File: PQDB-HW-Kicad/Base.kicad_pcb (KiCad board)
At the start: 2 copper layers, 146.1 x 141 mm, 71 parts, among them Q101 BC847, Q102 BC847, Q201 BC847, Q301 BC847, Q302 BC847, Q303 BC847, Q304 BC847, SW101 BTN-01, SW102 BTN-01, SW103 BTN-01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

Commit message: Add files via upload
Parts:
- added G***: LOGO, bibliotecas:OSHW_GRANDE, F.Cu at (181.5, 104.6)
- added P101: EXT_I2C, bibliotecas:EXT_I2C, F.Cu at (65.8, 139.1)
- added R105: 1k, bibliotecas:HW_Resistor, F.Cu at (107.7, 126.7)
- added R106: 1k, bibliotecas:HW_Resistor, F.Cu at (154.7, 126.7)
- G***: moved to F.Cu
- RV201, RV401: value POT -> POT_DUPLO; footprint HW_Potenciometro_2 -> bibliotecas:HW_Potenciometro_2_Duplo
- X701: footprint Crystals:Crystal_Round_Horizontal_2mm -> bibliotecas:Crystal_Round_Horizontal_2mm
- moved G*** 12.7 mm to (181.2, 82.4)
- moved R503 7.83 mm to (162.2, 45.3)
- moved R502 7.78 mm to (166.4, 45.3)
- moved R501 7.77 mm to (170.7, 45.3)
- moved RGB501 6.21 mm to (165.7, 34.9)
- moved Q101 6.08 mm to (72.5, 147.1)
- moved BZ201 5.17 mm to (194.2, 31.7)
- moved R201 5.14 mm to (183.2, 47.4)
- moved C701 4.45 mm to (83.1, 125.6)
- moved U401 4.41 mm to (75.8, 32.1)
- moved R407 4.22 mm to (168.5, 29.7)
- moved R301 3.02 mm to (126.9, 83.4)
- moved R312 2.95 mm to (126.8, 63.5)
- moved R305 2.94 mm to (126.9, 100.4)
- moved R306 2.94 mm to (126.9, 104.2)
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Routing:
- net +5V: track 416.2 -> 461.6 mm
- net /SDA: track 84.4 -> 118.6 mm
- net GND: track 1193.9 -> 1226.8 mm
- net /SCL: track 82.4 -> 115.2 mm
- net Net-(R103-Pad2): track 117.1 -> 134.9 mm
- net /DSP-1: track 40.7 -> 55.4 mm
- net Net-(R104-Pad2): track 116.7 -> 130.0 mm
- net /DSP-2: track 47.8 -> 59.0 mm
- net /DSP-3: track 50.6 -> 61.5 mm
- net /D3: track 179.6 -> 172.1 mm
- net /AN2: track 42.1 -> 49.1 mm
- net /D1: track 99.1 -> 92.8 mm
- net /D2: track 98.8 -> 92.5 mm
- net /D0: track 109.3 -> 103.4 mm
- net /PWM: track 12.4 -> 17.6 mm
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- added copper zone on B.Cu, net (none)
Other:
- board size 146.1 x 141 mm -> 147.2 x 146.8 mm
- net class Default: clearance 0.762 -> 0.5
- rule trace_clearance: 0.762 -> 0.5
- board text added: "(SCL)AD5 (SDA)AD4 AD3 AD2 AD1 AD0"
- board text added: "5V GND SDA SCL"
- board text added: "AD0"
- board text added: "AD1"
- board text added: "AD2"
- board text added: "AD5 AD4"
- board text added: "D2(DSP-1) D3(DSP-2) D4(DSP-3)"
- board text added: "D2(DSP-1) D3(DSP-2) D4(DSP-3) D5(DSP-4) D6(EnLCD) D7(lcdRS)"
- board text added: "D6(EnLCD)"
- board text added: "D7(lcdRS)"
- board text added: "D8(PWM)"
- board text added: "D8(soData) D10(PEn) D11(soClk)"
- board text added: "D8(soData) D9(PWM) D10(PEn) D11(soClk) D12(T2) D13(T1)"
- board text added: "DSP-1 DSP-2 DSP-3 DSP-4"
- board text added: "I2C Extension"
- board text added: "LEDS -> d0 à d7"
- board text added: "Licensed under CERN OHL v.1.2"
- board text added: "PQ DB"
- board text added: "d0"
- board text added: "d1"
- board text added: "d1 d2 d3 d4 d5 d6 d7"
- board text added: "d2"
- board text added: "d3"
- board text added: "d4"
- board text added: "d5"
- board text added: "d7"
- board text removed: "Kit de Desenvolvimento pqdb v1.0 Unifei 2016 Licensed under CERN OHL v.1.2"

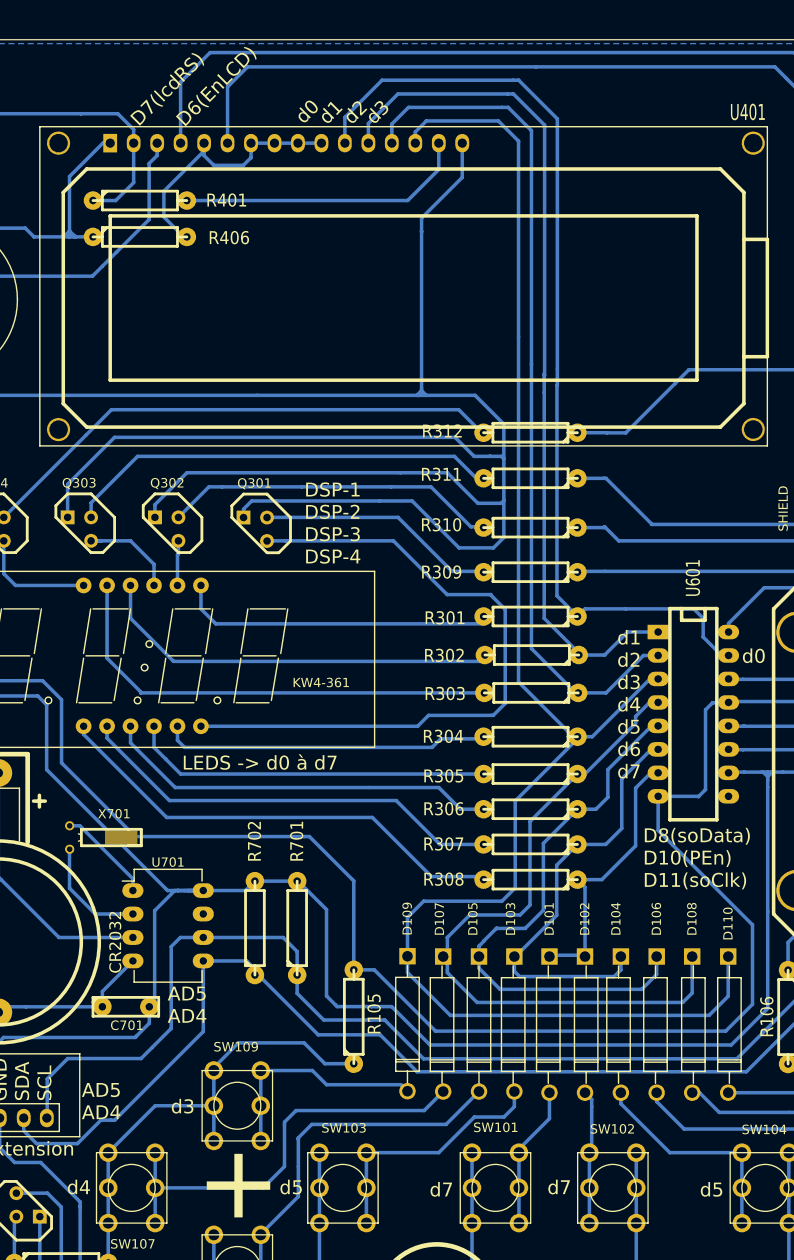
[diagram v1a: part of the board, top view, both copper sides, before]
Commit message: Silk screen update
Corrigida referencia do silk nos botões.
Adiçào das referências dos componentes na camada de silk.
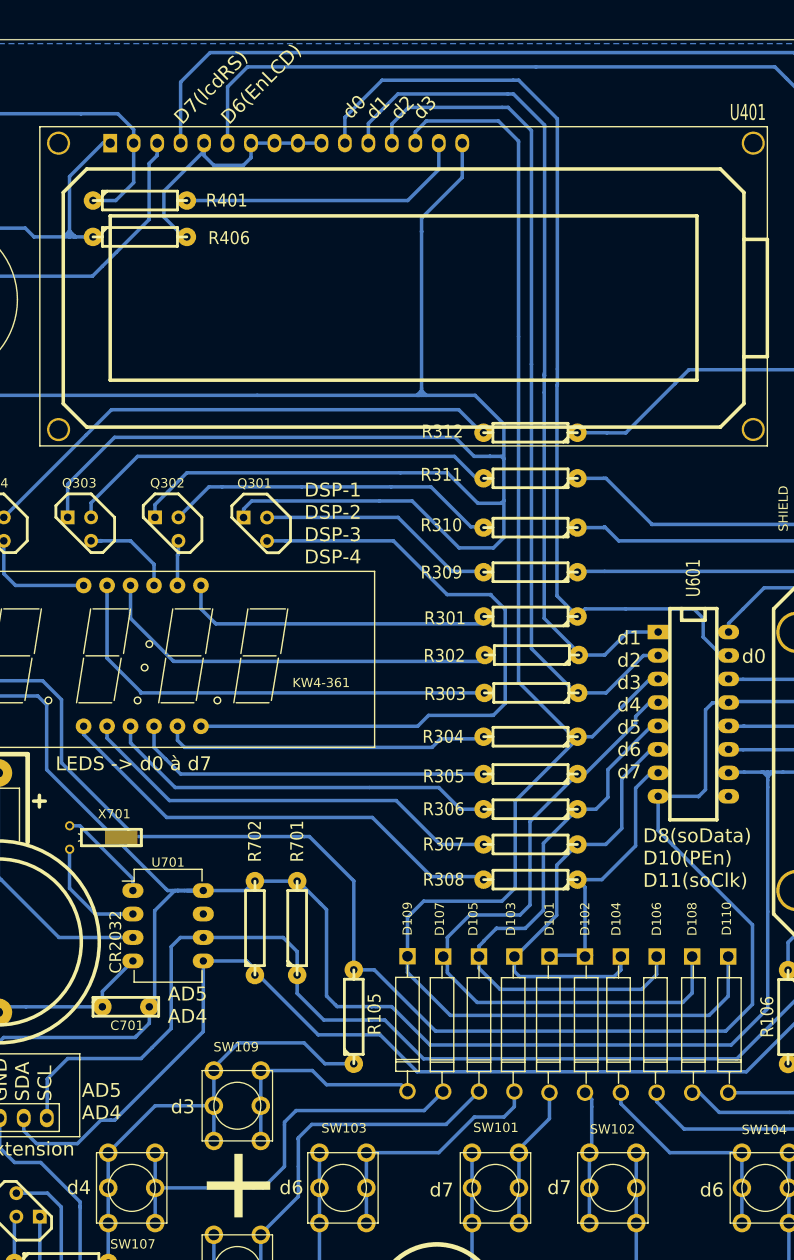
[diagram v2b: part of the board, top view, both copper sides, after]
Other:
- board text added: "d6"
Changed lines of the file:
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@@
-(kicad_pcb (version 4) (host pcbnew 4.0.6)
+(kicad_pcb (version 4) (host pcbnew 4.0.7)
   (general
     (links 192)
     (no_connects 2)
-    (area 45.744499 20.7228 222.492 167.767001)
+    (area 45.744499 20.502883 222.492 167.767001)
     (thickness 1.6)
     (drawings 54)
@@
     (visible_elements 7FFEFFFF)
     (pcbplotparams
-      (layerselection 0x01064_80000000)
+      (layerselection 0x00020_00000000)
       (usegerberextensions false)
       (excludeedgelayer true)
@@
       (psnegative false)
       (psa4output false)
-      (plotreference false)
+      (plotreference true)
       (plotvalue false)
       (plotinvisibletext false)
@@
     (descr "Diode 5 pas")
     (tags "DIODE DEV")
-    (fp_text reference D110 (at -10.922 0.127 270) (layer F.SilkS)
+    (fp_text reference D110 (at -11.464 0.296 270) (layer F.SilkS)
       (effects (font (size 1 1) (thickness 0.15)))
     )
@@
     )
   )
-  (gr_text d2 (at 106.9975 29.718 45) (layer F.SilkS)
+  (gr_text d2 (at 112.0775 29.21 45) (layer F.SilkS)
     (effects (font (size 1.5 1.5) (thickness 0.25)) (justify left))
   )
-  (gr_text d1 (at 104.3305 29.718 45) (layer F.SilkS)
+  (gr_text d1 (at 109.4105 29.21 45) (layer F.SilkS)
     (effects (font (size 1.5 1.5) (thickness 0.25)) (justify left))
   )
-  (gr_text d0 (at 101.7905 29.6545 45) (layer F.SilkS)
+  (gr_text d0 (at 106.8705 29.1465 45) (layer F.SilkS)
     (effects (font (size 1.5 1.5) (thickness 0.25)) (justify left))
   )
-  (gr_text "D6(EnLCD)" (at 88.9 29.972 45) (layer F.SilkS)
+  (gr_text "D6(EnLCD)" (at 93.726 29.718 45) (layer F.SilkS)
     (effects (font (size 1.5 1.5) (thickness 0.25)) (justify left))
   )
-  (gr_text "D7(lcdRS)" (at 83.947 29.9085 45) (layer F.SilkS)
+  (gr_text "D7(lcdRS)" (at 88.646 29.718 45) (layer F.SilkS)
     (effects (font (size 1.5 1.5) (thickness 0.25)) (justify left))
   )
-  (gr_text "LEDS -> d0 à d7" (at 89.128 99.242) (layer F.SilkS)
+  (gr_text "LEDS -> d0 à d7" (at 75.438 99.314) (layer F.SilkS)
     (effects (font (size 1.5 1.5) (thickness 0.25)) (justify left))
   )
@@
     (effects (font (size 1.5 1.5) (thickness 0.25)) (justify left))
   )
-  (gr_text d3 (at 109.4105 29.718 45) (layer F.SilkS)
+  (gr_text d3 (at 114.4905 29.21 45) (layer F.SilkS)
     (effects (font (size 1.5 1.5) (thickness 0.25)) (justify left))
   )
@@
     (effects (font (size 1.5 1.5) (thickness 0.25)))
   )
-  (gr_text d5 (at 146.478 145.442) (layer F.SilkS)
+  (gr_text d6 (at 146.478 145.442) (layer F.SilkS)
     (effects (font (size 1.5 1.5) (thickness 0.25)))
   )
@@
     (effects (font (size 1.5 1.5) (thickness 0.25)))
   )
-  (gr_text d5 (at 100.978 145.192) (layer F.SilkS)
+  (gr_text d6 (at 100.978 145.192) (layer F.SilkS)
     (effects (font (size 1.5 1.5) (thickness 0.25)))
   )
